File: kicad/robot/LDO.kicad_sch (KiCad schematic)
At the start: 0 parts

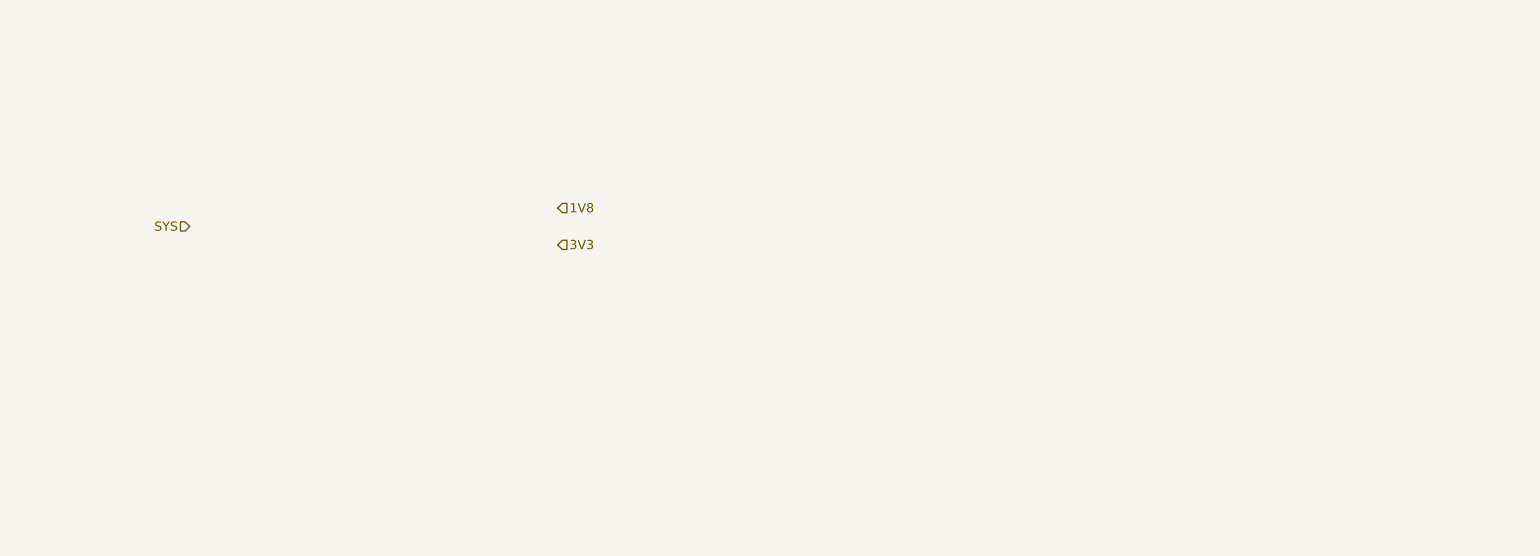
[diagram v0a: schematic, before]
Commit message: Added LDO schematic
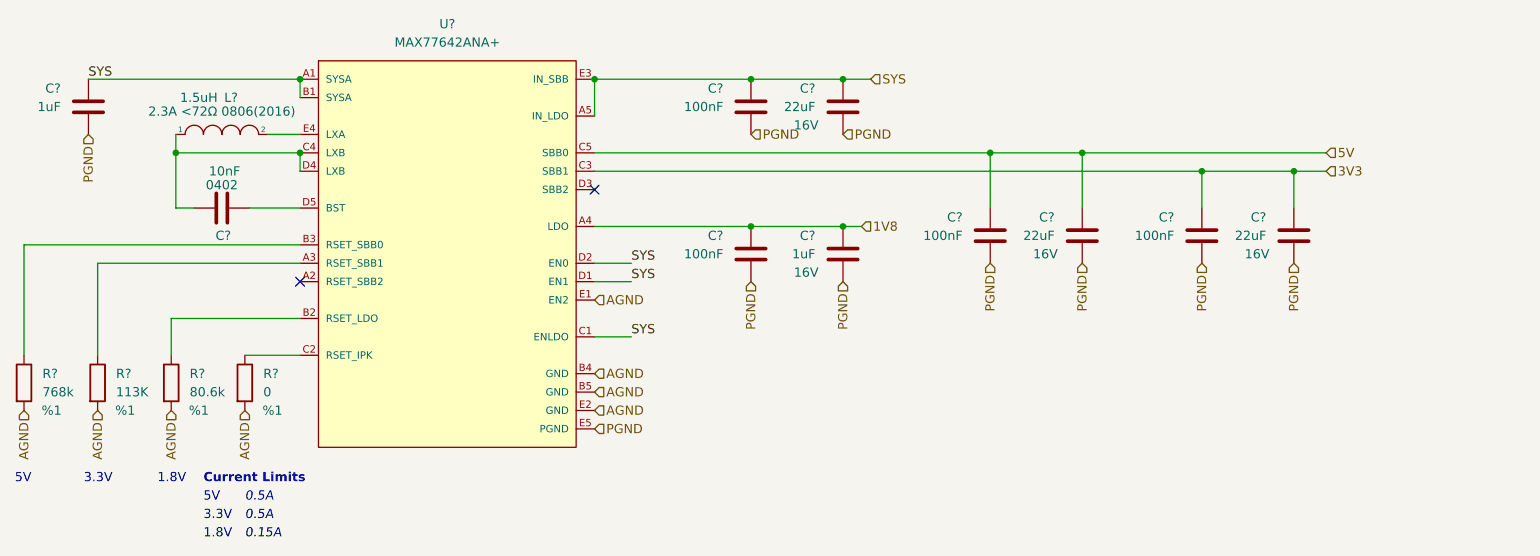
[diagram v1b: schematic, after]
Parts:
- added C? (x3): 22uF, symbol Device:C
- added C? (x2): 1uF, symbol Device:C
- added C? (x4): 100nF, symbol Device:C
- added C?: 10nF, symbol Device:C
- added L?: 1.5uH, symbol pspice:INDUCTOR
- added R?: 113K, symbol Device:R
- added R?: 80.6k, symbol Device:R
- added R?: 0, symbol Device:R
- added R?: 768k, symbol Device:R
- added U?: MAX77642ANA+, Package_BGA:Maxim-N252B2-1-0-A-MFG, symbol Regulator_Switching:MAX77642ANA+
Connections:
- net 1V8: now also C?.1, C?.1, U?.A4 (LDO)
- net 3V3: now also C?.1, C?.1, U?.C3 (SBB1)
- net SYS: now also C?.1, C?.1, C?.1, U?.A1 (SYSA), U?.A5 (IN_LDO), U?.B1 (SYSA), U?.C1 (ENLDO), U?.D1 (EN1), U?.D2 (EN0), U?.E3 (IN_SBB)
- new net: R?.1, U?.A3 (RSET_SBB1)
- new net: R?.1, U?.B2 (RSET_LDO)
- new net: R?.1, U?.B3 (RSET_SBB0)
- new net: R?.1, U?.C2 (RSET_IPK)
- new net: C?.1, L?.1, U?.C4 (LXB), U?.D4 (LXB)
- new net: C?.2, U?.D5 (BST)
- new net: L?.2, U?.E4 (LXA)
- new net 5V: C?.1, C?.1, U?.C5 (SBB0)
- new net AGND: R?.2, R?.2, R?.2, R?.2, U?.B4 (GND), U?.B5 (GND), U?.E1 (EN2), U?.E2 (GND)
- new net PGND: C?.2, C?.2, C?.2, C?.2, C?.2, C?.2, C?.2, C?.2, C?.2, U?.E5 (PGND)
- no-connect marks 0 -> 2
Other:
- note added: "0.15A"
- note added: "0.5A"
- note added: "1.8V"
- note added: "3.3V"
- note added: "5V"
- note added: "Current Limits"

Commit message: Assigned resistor footprints
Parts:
- R? (x4): footprint (none) -> Resistor_SMD:R_0603_1608Metric
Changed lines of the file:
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@@
       (effects (font (size 1.27 1.27)) (justify left))
     )
-    (property "Footprint" "" (id 2) (at 66.802 118.11 90)
+    (property "Footprint" "Resistor_SMD:R_0603_1608Metric" (id 2) (at 66.802 118.11 90)
       (effects (font (size 1.27 1.27)) hide)
     )
@@
       (effects (font (size 1.27 1.27)) (justify left))
     )
-    (property "Footprint" "" (id 2) (at 76.962 118.11 90)
+    (property "Footprint" "Resistor_SMD:R_0603_1608Metric" (id 2) (at 76.962 118.11 90)
       (effects (font (size 1.27 1.27)) hide)
     )
@@
       (effects (font (size 1.27 1.27)) (justify left))
     )
-    (property "Footprint" "" (id 2) (at 87.122 118.11 90)
+    (property "Footprint" "Resistor_SMD:R_0603_1608Metric" (id 2) (at 87.122 118.11 90)
       (effects (font (size 1.27 1.27)) hide)
     )
@@
       (effects (font (size 1.27 1.27)) (justify left))
     )
-    (property "Footprint" "" (id 2) (at 56.642 118.11 90)
-      (effects (font (size 1.27 1.27)) hide)
-    )
+    (property "Footprint" "Resistor_SMD:R_0603_1608Metric" (id 2) (at 56.642 118.11 90)
+      (effects (font (size 1.27 1.27)) hide)
+    )

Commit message: Assigned capacitor footprints
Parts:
- C? (x9): footprint (none) -> Capacitor_SMD:C_0603_1608Metric
- C?: footprint (none) -> Capacitor_SMD:C_0402_1005Metric
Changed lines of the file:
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@@
       (effects (font (size 1.27 1.27)) (justify left))
     )
-    (property "Footprint" "" (id 2) (at 232.7148 101.6 0)
+    (property "Footprint" "Capacitor_SMD:C_0603_1608Metric" (id 2) (at 232.7148 101.6 0)
       (effects (font (size 1.27 1.27)) hide)
     )
@@
       (effects (font (size 1.27 1.27)) (justify left))
     )
-    (property "Footprint" "" (id 2) (at 170.4848 104.14 0)
+    (property "Footprint" "Capacitor_SMD:C_0603_1608Metric" (id 2) (at 170.4848 104.14 0)
       (effects (font (size 1.27 1.27)) hide)
     )
@@
       (effects (font (size 1.27 1.27)) (justify left))
     )
-    (property "Footprint" "" (id 2) (at 170.4848 83.82 0)
+    (property "Footprint" "Capacitor_SMD:C_0603_1608Metric" (id 2) (at 170.4848 83.82 0)
       (effects (font (size 1.27 1.27)) hide)
     )
@@
       (effects (font (size 1.27 1.27)) (justify left))
     )
-    (property "Footprint" "" (id 2) (at 157.7848 104.14 0)
+    (property "Footprint" "Capacitor_SMD:C_0603_1608Metric" (id 2) (at 157.7848 104.14 0)
       (effects (font (size 1.27 1.27)) hide)
     )
@@
       (effects (font (size 1.27 1.27)) (justify left))
     )
-    (property "Footprint" "" (id 2) (at 157.7848 83.82 0)
+    (property "Footprint" "Capacitor_SMD:C_0603_1608Metric" (id 2) (at 157.7848 83.82 0)
       (effects (font (size 1.27 1.27)) hide)
     )
@@
       (effects (font (size 1.27 1.27)) (justify left))
     )
-    (property "Footprint" "" (id 2) (at 66.3448 83.82 0)
+    (property "Footprint" "Capacitor_SMD:C_0603_1608Metric" (id 2) (at 66.3448 83.82 0)
       (effects (font (size 1.27 1.27)) hide)
     )
@@
       (effects (font (size 1.27 1.27)) (justify left))
     )
-    (property "Footprint" "" (id 2) (at 220.0148 101.6 0)
+    (property "Footprint" "Capacitor_SMD:C_0603_1608Metric" (id 2) (at 220.0148 101.6 0)
       (effects (font (size 1.27 1.27)) hide)
     )
@@
       (effects (font (size 1.27 1.27)) (justify left))
     )
-    (property "Footprint" "" (id 2) (at 203.5048 101.6 0)
+    (property "Footprint" "Capacitor_SMD:C_0603_1608Metric" (id 2) (at 203.5048 101.6 0)
       (effects (font (size 1.27 1.27)) hide)
     )
@@
       (effects (font (size 1.27 1.27)) (justify left))
     )
-    (property "Footprint" "" (id 2) (at 190.8048 101.6 0)
+    (property "Footprint" "Capacitor_SMD:C_0603_1608Metric" (id 2) (at 190.8048 101.6 0)
       (effects (font (size 1.27 1.27)) hide)
     )
@@
       (effects (font (size 1.27 1.27)) (justify left))
     )
-    (property "Footprint" "" (id 2) (at 89.535 94.9452 0)
-      (effects (font (size 1.27 1.27)) hide)
-    )
+    (property "Footprint" "Capacitor_SMD:C_0402_1005Metric" (id 2) (at 89.535 94.9452 0)
+      (effects (font (size 1.27 1.27)) hide)
+    )

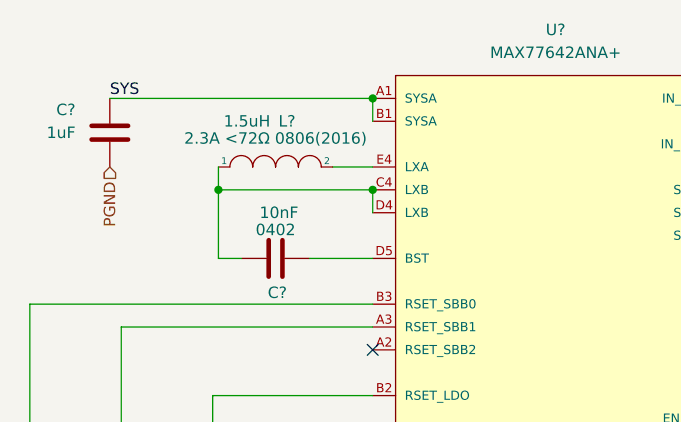
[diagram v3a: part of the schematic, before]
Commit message: Assigned inductor footprints
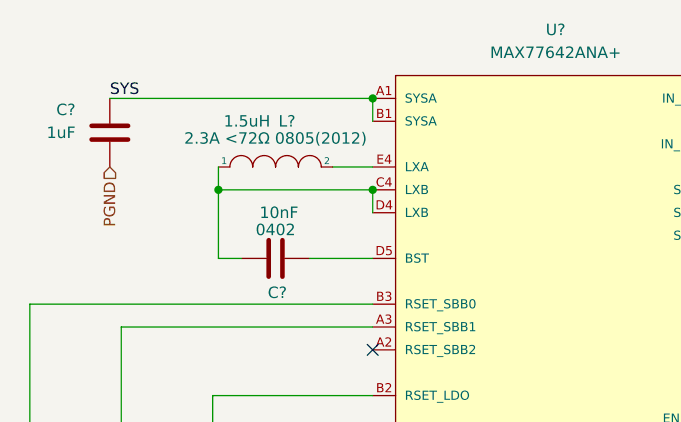
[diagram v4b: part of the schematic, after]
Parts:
- L?: footprint (none) -> Inductor_SMD:L_0805_2012Metric
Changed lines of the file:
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@@
     (property "Reference" "L?" (id 0) (at 86.995 78.74 0))
     (property "Value" "1.5uH" (id 1) (at 82.55 78.74 0))
-    (property "Footprint" "" (id 2) (at 85.725 83.82 0)
+    (property "Footprint" "Inductor_SMD:L_0805_2012Metric" (id 2) (at 85.725 83.82 0)
       (effects (font (size 1.27 1.27)) hide)
     )
@@
       (effects (font (size 1.27 1.27)) hide)
     )
-    (property "Description" "2.3A <72Ω 0806(2016)" (id 4) (at 85.725 80.645 0))
+    (property "Description" "2.3A <72Ω 0805(2012)" (id 4) (at 85.725 80.645 0))
     (pin "1")
     (pin "2")

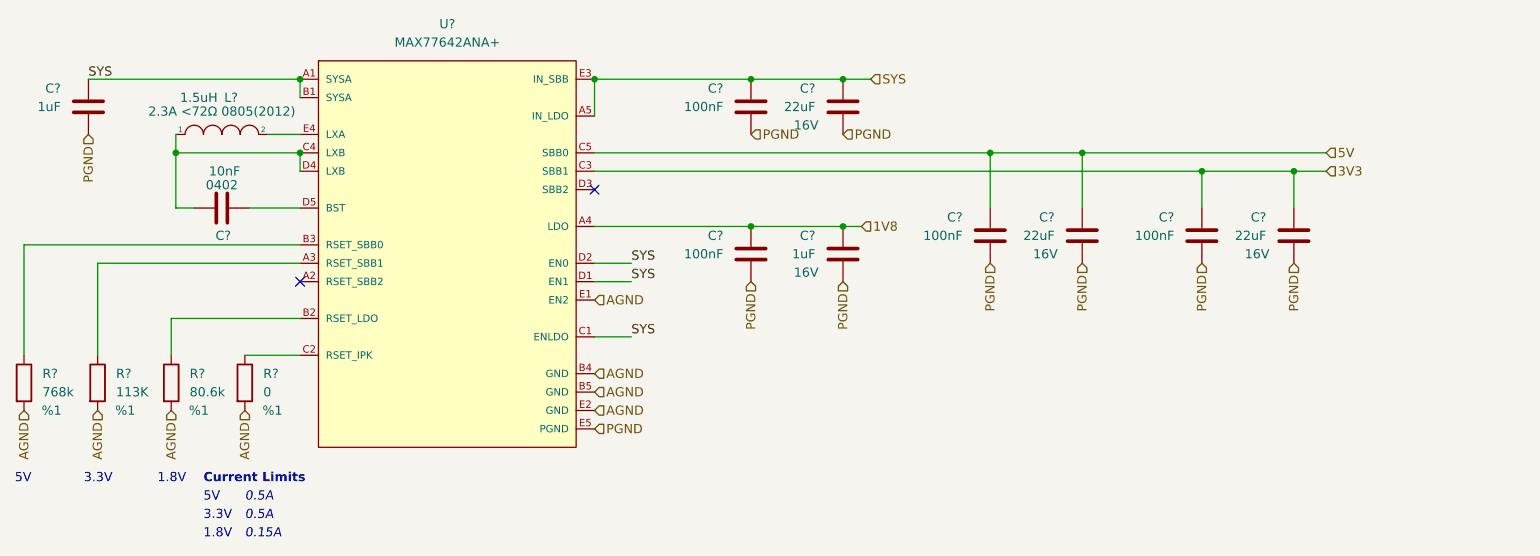
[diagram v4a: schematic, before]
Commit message: Added 1uF cap to SBB2 according to datasheet requirements
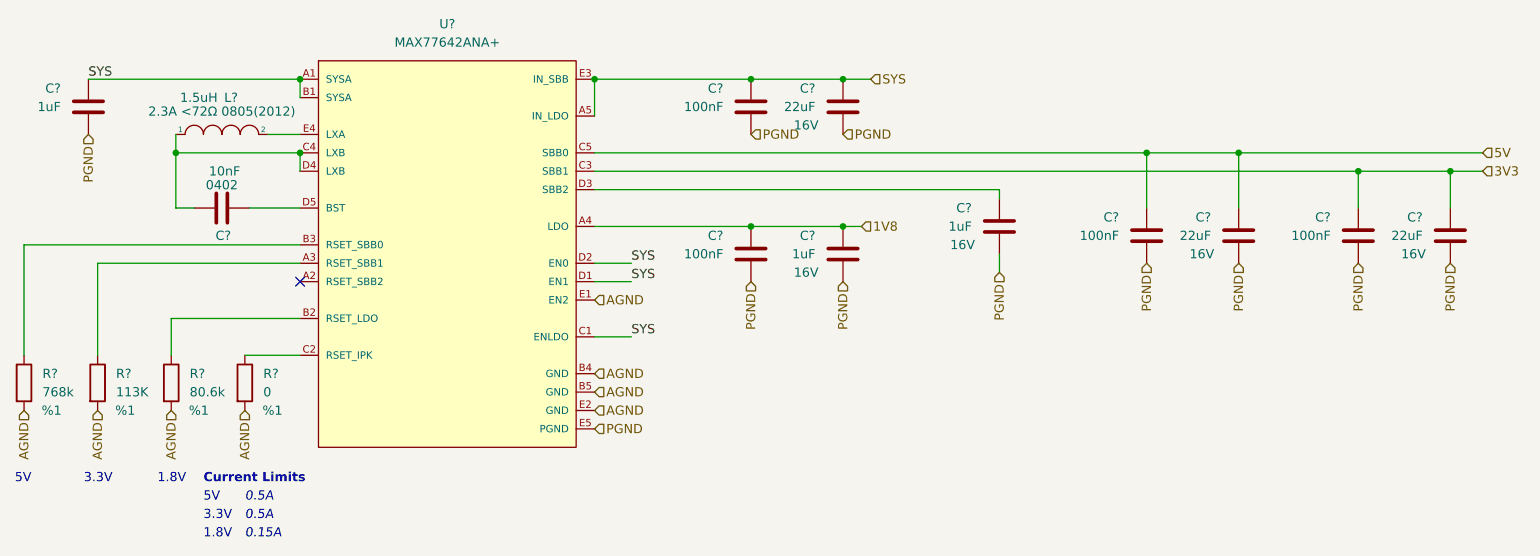
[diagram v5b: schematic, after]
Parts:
- added C?: 1uF, Capacitor_SMD:C_0603_1608Metric, symbol Device:C
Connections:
- net PGND: now also C?.2
- net at U?.D3 (SBB2): now also C?.1
- no-connect marks 2 -> 1
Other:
- moved on the sheet: C?

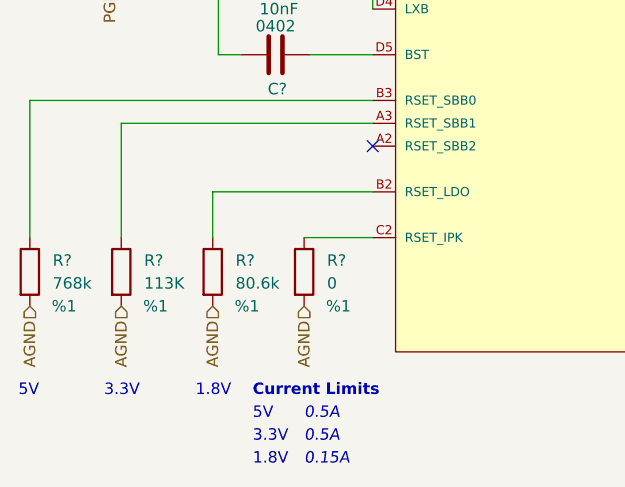
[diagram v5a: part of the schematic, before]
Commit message: Correct RSET resistance for 3V3 and 1V8 pins on simo
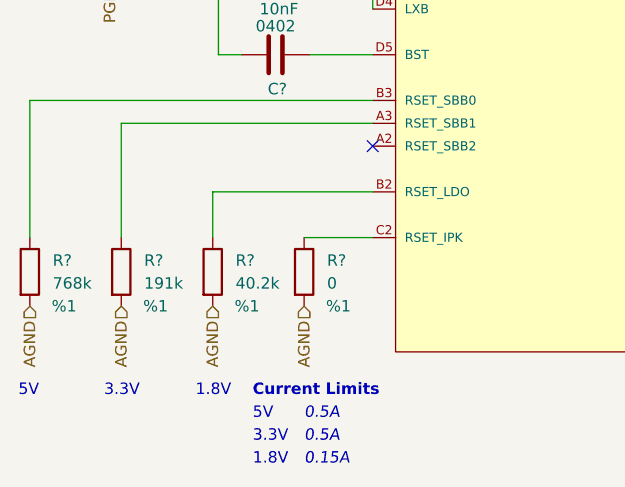
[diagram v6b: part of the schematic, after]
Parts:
- R?: value 113K -> 191k
- R?: value 80.6k -> 40.2k
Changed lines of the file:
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@@
       (effects (font (size 1.27 1.27)) (justify left))
     )
-    (property "Value" "113K" (id 1) (at 71.12 119.3799 0)
+    (property "Value" "191k" (id 1) (at 71.12 119.3799 0)
       (effects (font (size 1.27 1.27)) (justify left))
     )
@@
       (effects (font (size 1.27 1.27)) (justify left))
     )
-    (property "Value" "80.6k" (id 1) (at 81.28 119.3799 0)
-      (effects (font (size 1.27 1.27)) (justify left))
-    )
+    (property "Value" "40.2k" (id 1) (at 81.28 119.3799 0)
+      (effects (font (size 1.27 1.27)) (justify left))
+    )

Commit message: Revert "Correct RSET resistance for 3V3 and 1V8 pins on simo"
This reverts commit 3c014a89efb1627164809f39dad8e492ec139191.
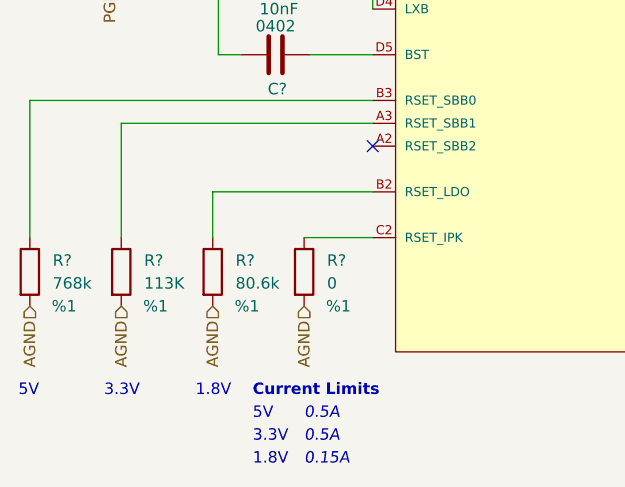
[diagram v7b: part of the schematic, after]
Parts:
- R?: value 191k -> 113K
- R?: value 40.2k -> 80.6k
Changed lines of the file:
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@@
       (effects (font (size 1.27 1.27)) (justify left))
     )
-    (property "Value" "191k" (id 1) (at 71.12 119.3799 0)
+    (property "Value" "113K" (id 1) (at 71.12 119.3799 0)
       (effects (font (size 1.27 1.27)) (justify left))
     )
@@
       (effects (font (size 1.27 1.27)) (justify left))
     )
-    (property "Value" "40.2k" (id 1) (at 81.28 119.3799 0)
-      (effects (font (size 1.27 1.27)) (justify left))
-    )
+    (property "Value" "80.6k" (id 1) (at 81.28 119.3799 0)
+      (effects (font (size 1.27 1.27)) (justify left))
+    )

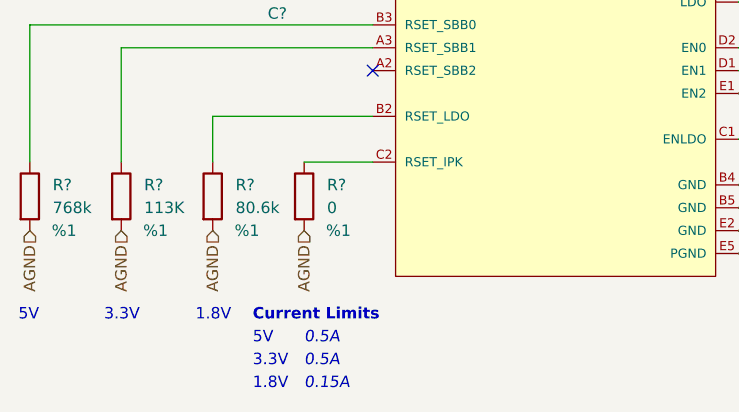
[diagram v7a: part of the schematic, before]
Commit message: Updated RESET_IPK to 14k to allow higher current limits and <100% inductor utilization from xls sheet
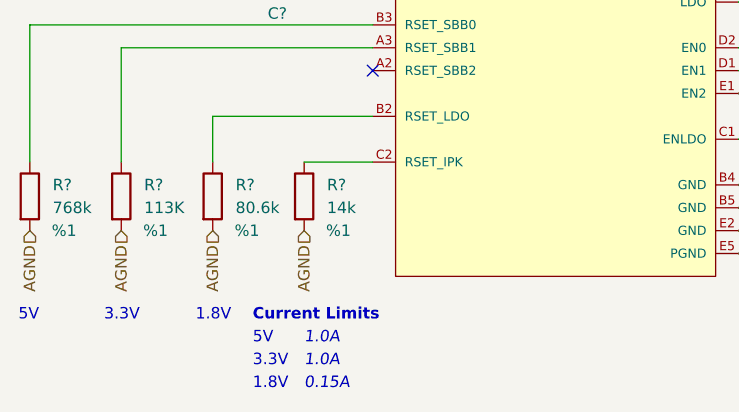
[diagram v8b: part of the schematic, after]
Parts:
- R?: value 0 -> 14k
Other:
- note added: "1.0A"
- note removed: "0.5A"
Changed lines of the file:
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@@
     (effects (font (size 1.27 1.27)) (justify left bottom))
   )
-  (text "0.5A" (at 88.9 137.16 0)
+  (text "1.0A" (at 88.9 137.16 0)
     (effects (font (size 1.27 1.27) italic) (justify left bottom))
   )
-  (text "0.5A" (at 88.9 134.62 0)
+  (text "1.0A" (at 88.9 134.62 0)
     (effects (font (size 1.27 1.27) italic) (justify left bottom))
   )
@@
       (effects (font (size 1.27 1.27)) (justify left))
     )
-    (property "Value" "0" (id 1) (at 91.44 119.3799 0)
-      (effects (font (size 1.27 1.27)) (justify left))
-    )
+    (property "Value" "14k" (id 1) (at 91.44 119.3799 0)
+      (effects (font (size 1.27 1.27)) (justify left))
+    )
